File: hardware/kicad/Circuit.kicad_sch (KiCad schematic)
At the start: 10 parts, among them J1 TYPE-C-31-M-12, U1 ESP32-C6-WROOM-1-N8, U2 BME680, U3 BQ24075RGT

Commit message: hardware: power section & components
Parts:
- removed U2: BME680, BME680:PSON80P300X300X100-8N, symbol SnapEDA-Library:BME680
- added C10: 22uF, PCM_JLCPCB:C_0603, symbol Device:C
- added C2: 100nF, PCM_JLCPCB:C_0603, symbol Device:C
- added C3, C4, C8, C9: 10uF, PCM_JLCPCB:C_0603, symbol Device:C
- added C5, C7: 4.7uF, PCM_JLCPCB:C_0603, symbol Device:C
- added C6: 1uF, PCM_JLCPCB:C_0603, symbol Device:C
- added D3, D6, D7, D8: LESD5D5.0CT1G, LESD5D5.0CT1G:TVS_LESD5D5.0CT1G, symbol LESD5D5.0CT1G:LESD5D5.0CT1G
- added D4: 1N5819HW-7-F, 1N5819HW-7-F:SOD3715X145N, symbol 1N5819HW-7-F:1N5819HW-7-F
- added D5: Red, PCM_JLCPCB:D_0603, symbol PCM_JLCPCB-Diodes:LED,0603,Red
- added D9: Green, PCM_JLCPCB:D_0603, symbol PCM_JLCPCB-Diodes:LED,0603,Red
- added J2: B2B-XH-A__LF__SN_, B2B-XH-A__LF__SN_:JST_B2B-XH-A__LF__SN_, symbol B2B-XH-A__LF__SN_:B2B-XH-A__LF__SN_
- added L1: 1.5uH, Inductor_SMD:L_0603_1608Metric, symbol Device:L
- added R10: 470K, PCM_JLCPCB:R_0603, symbol Device:R
- added R11: 150K, PCM_JLCPCB:R_0603, symbol Device:R
- added R12: R, PCM_JLCPCB:R_0603, symbol Device:R
- added R4: 887, PCM_JLCPCB:R_0603, symbol Device:R
- added R5: 1.1K, PCM_JLCPCB:R_0603, symbol Device:R
- added R6, R9: 5k1, PCM_JLCPCB:R_0603, symbol Device:R
- added R7, R8: 1.5K, PCM_JLCPCB:R_0603, symbol Device:R
- added TH1: 10K, Resistor_SMD:R_0603_1608Metric, symbol Device:Thermistor_NTC
- added U4: TPS63070RNMR, TPS63070RNMR:VREG_TPS63070RNMR, symbol TPS63070RNMR:TPS63070RNMR
- added U5: BME680, BME680:PSON80P300X300X100-8N, symbol BME680:BME680
- R2: value 5k1 -> R
- R3: value 5k1 -> 10K
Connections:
- net VBUS is gone; now on net +5V: J1.A4_B9 (VBUS), J1.B4_A9 (VBUS)
- net GND: now also U3.14 (TMR), U3.15 (SYSOFF), U3.17 (VSS), U3.4 (~{CE}), U3.6 (EN1), U3.8 (VSS), C10.2, C2.2, C3.1, C4.2, C5.2, C6.2, C7.1, C8.2, C9.2, D6.1, D7.1, D8.1, J2.2, R11.2, R4.1, R5.1, R6.2, R9.2, TH1.2, U4.10 (PGND), U4.15 (VSEL), U4.4 (GND), U4.6 (FB2), U5.1 (GND), U5.7 (GND); no longer R2.2, R3.2
- net TS: now reaches U3.1 (TS)
- net TS: now also TH1.1
- net OUT: now reaches U3.10 (OUT), U3.11 (OUT)
- net OUT: now also R3.1, C4.1, C5.1, C8.1, D5.2, D9.2, U4.12_13 (VIN)
- net at U3.12 (ILIM): now also R5.2
- net +5V: now reaches U3.13 (IN)
- net +5V: now also U3.5 (EN2), C3.2, C6.1, C7.2, D6.2
- net at U3.16 (ISET): now also R4.2
- net BAT: now reaches U3.2 (BAT), U3.3 (BAT)
- net BAT: now also J2.1
- net ~{PGOOD}: now reaches U3.7 (~{PGOOD})
- net ~{PGOOD}: now also R8.2
- net ~{CHG}: now reaches U3.9 (~{CHG})
- net ~{CHG}: now also R7.2
- net at R2.1: no longer J1.A5 (CC1)
- net D+: now reaches J1.A6 (DP1), J1.B6 (DP2)
- net D+: now also D8.2
- net D-: now reaches J1.A7 (DN1), J1.B7 (DN2)
- net D-: now also D7.2
- net CC2: now reaches J1.B5 (CC2)
- net CC2: now also R6.1; no longer R3.1
- new net: D5.1, R7.1
- new net: L1.2, U4.11 (L1)
- new net: C2.1, U4.3 (VAUX)
- new net: L1.1, U4.9 (L2)
- new net: D9.1, R8.1
- new net +3.3V: C10.1, C9.1, R10.1, R12.1, U4.7_8 (VOUT)
- new net CC1: J1.A5 (CC1), R9.1
- new net EN: R3.2, U4.1 (PS/SYNC), U4.14 (EN)
- new net FB: R10.2, R11.1, U4.5 (FB)
- new net PG: R12.2, U4.2 (PG)
- no-connect marks 0 -> 2
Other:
- note added: "1N5819HW-7-F not needed, BQ24075RGT is equiped with reverse current protecion on IN pin"
- note added: "Battery connector"
- note added: "Battery current limited to 500 mA"
- note added: "Buck boost converter"
- note added: "Check pins of battery, change polarization if needed"
- note added: "Dynamic Power Path Management"
- note added: "Enviroment sensor"
- note added: "Input current limited to 1500 mA"
- note added: "MCU"
- note added: "Max operating current 3A"
- note added: "On battery connector: JST SYP-02T-1"
- note added: "Output = 3.3V"
- note added: "R4 Tollerance must be 1%"
- note added: "TH1 must be close to J2"
- note added: "Test point"
- note added: "USB-C"
- company: (none) -> Glitch Projects
- title: (none) -> Weather station
- moved on the sheet: C1, D1, D2, J1, R1, U1, U3

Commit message: hardware: MCU components
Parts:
- removed C1: C, PCM_JLCPCB:C_0603, symbol Device:C
- removed D1: 1N5819, Diode_THT:D_DO-41_SOD81_P10.16mm_Horizontal, symbol Diode:1N5819
- removed D2: Red, PCM_JLCPCB:D_0603, symbol PCM_JLCPCB-Diodes:LED,0603,Red
- removed D3: LESD5D5.0CT1G, LESD5D5.0CT1G:TVS_LESD5D5.0CT1G, symbol LESD5D5.0CT1G:LESD5D5.0CT1G
- removed D4: 1N5819HW-7-F, 1N5819HW-7-F:SOD3715X145N, symbol 1N5819HW-7-F:1N5819HW-7-F
- removed R1, R2: R, PCM_JLCPCB:R_0603, symbol Device:R
- removed U1: ESP32-C6-WROOM-1-N8, ESP32-C6-WROOM-1-N8:XCVR_ESP32-C6-WROOM-1-N8, symbol SnapEDA-Library:ESP32-C6-WROOM-1-N8
- removed U5: BME680, BME680:PSON80P300X300X100-8N, symbol BME680:BME680
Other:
- note removed: "Enviroment sensor"
- note removed: "MCU"

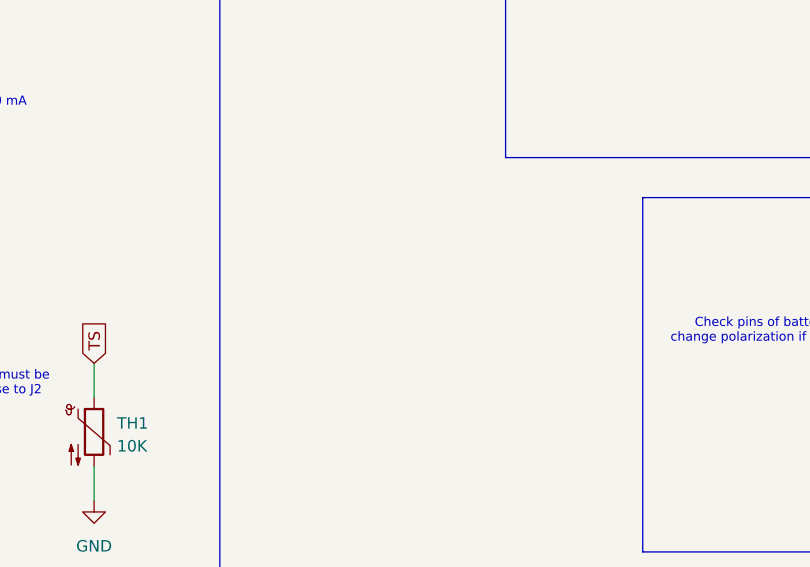
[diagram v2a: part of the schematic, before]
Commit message: hardware: movement sensor
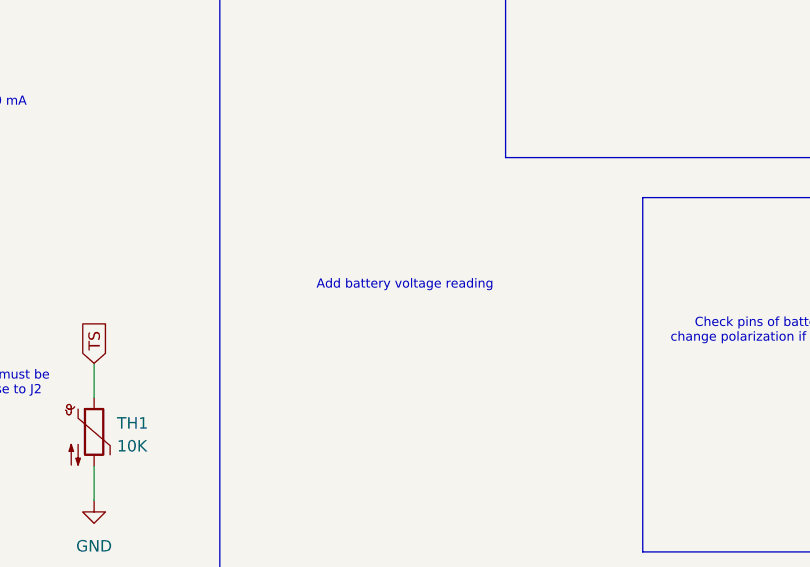
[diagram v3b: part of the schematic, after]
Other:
- note added: "Add battery voltage reading"
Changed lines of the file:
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@@
+		)
+	)
+	(text "Add battery voltage reading"
+		(exclude_from_sim yes)
+		(at 151.384 128.524 0)
+		(effects
+			(font
+				(size 1.016 1.016)
+			)
 		)
 	)

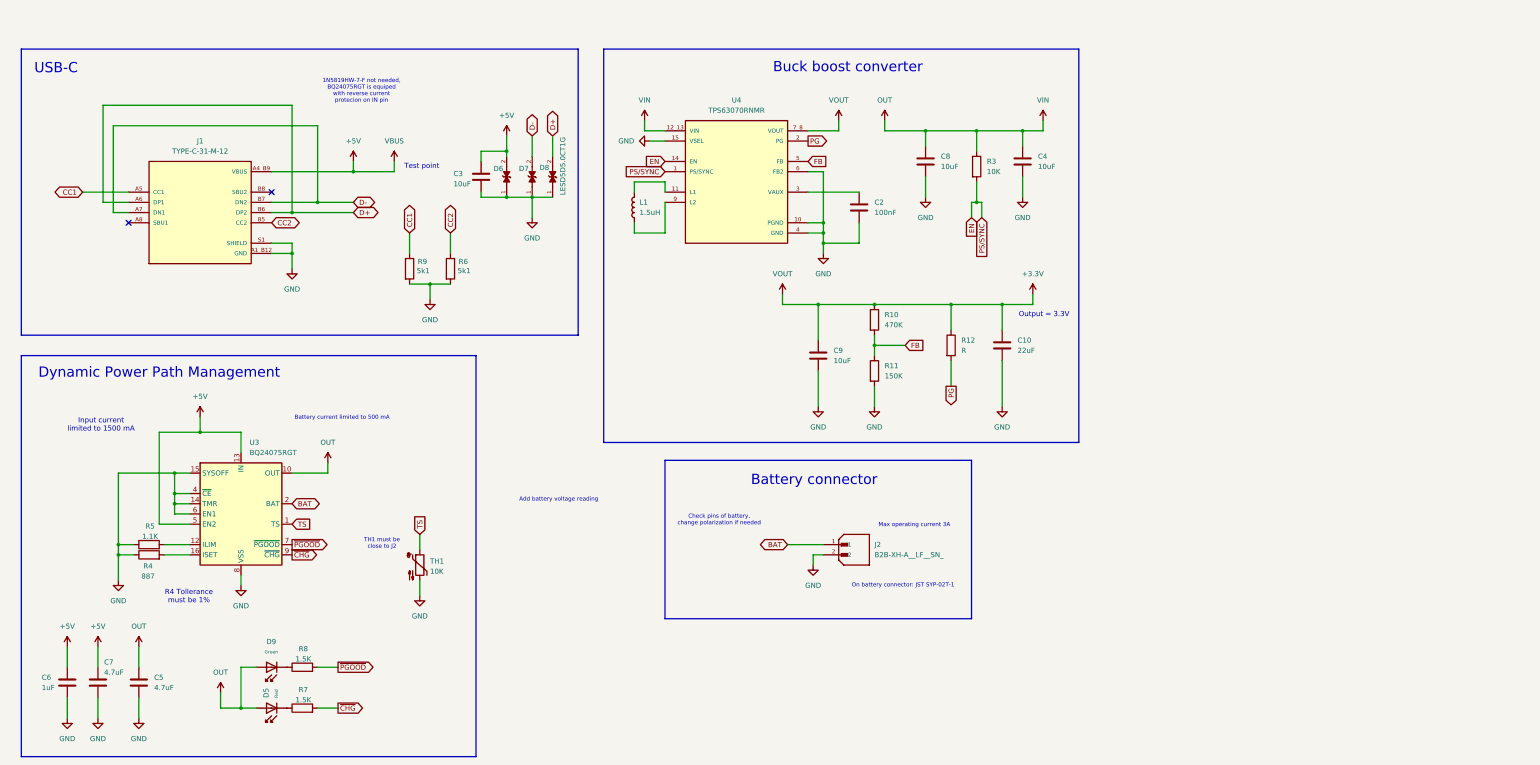
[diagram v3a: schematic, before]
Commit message: hardware: battery voltage reading and caps
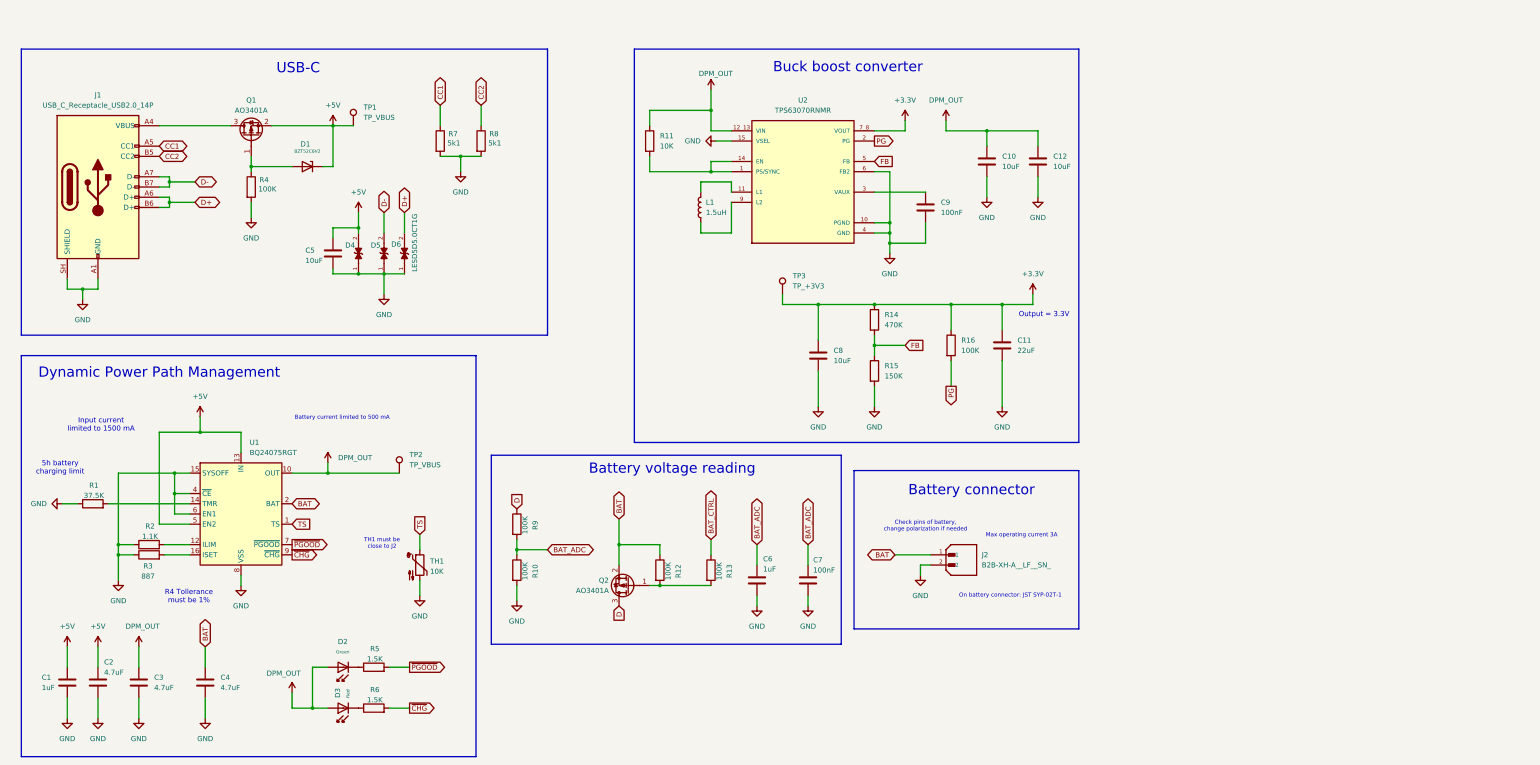
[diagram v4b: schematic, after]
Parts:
- removed J1: TYPE-C-31-M-12, TYPE-C-31-M-12:HRO_TYPE-C-31-M-12, symbol TYPE-C-31-M-12:TYPE-C-31-M-12
- added C4: 4.7uF, PCM_JLCPCB:C_0603, symbol Device:C
- added C6: 1uF, PCM_JLCPCB:C_0603, symbol Device:C
- added C7: 100nF, PCM_JLCPCB:C_0603, symbol Device:C
- added D1: BZT52C6V2, PCM_JLCPCB:D_SOD-123, symbol PCM_JLCPCB-Diodes:Zener,BZT52C6V2
- added J1: USB_C_Receptacle_USB2.0_14P, Connector_USB:USB_C_Receptacle_HRO_TYPE-C-31-M-12, symbol Connector:USB_C_Receptacle_USB2.0_14P
- added Q1, Q2: AO3401A, Package_TO_SOT_SMD:SOT-23, symbol Transistor_FET:AO3401A
- added R1: 37.5K, PCM_JLCPCB:R_0603, symbol Device:R
- added R10, R12, R13, R4, R9: 100K, PCM_JLCPCB:R_0603, symbol Device:R
- added TP1, TP2: TP_VBUS, TestPoint:TestPoint_Pad_D1.5mm, symbol Connector:TestPoint
- added TP3: TP_+3V3, TestPoint:TestPoint_Pad_D1.5mm, symbol Connector:TestPoint
- D4: renamed from D6; footprint LESD5D5.0CT1G:TVS_LESD5D5.0CT1G -> Diode_SMD:TVS_LESD5D5.0CT1G
- D5: renamed from D7; footprint LESD5D5.0CT1G:TVS_LESD5D5.0CT1G -> Diode_SMD:TVS_LESD5D5.0CT1G
- D6: renamed from D8; footprint LESD5D5.0CT1G:TVS_LESD5D5.0CT1G -> Diode_SMD:TVS_LESD5D5.0CT1G
- J2: footprint B2B-XH-A__LF__SN_:JST_B2B-XH-A__LF__SN_ -> Connector_JST:JST_B2B-XH-A__LF__SN_
- R16: renamed from R12; value R -> 100K
- U2: renamed from U4; footprint TPS63070RNMR:VREG_TPS63070RNMR -> Converter_DCDC:VREG_TPS63070RNMR
- renumbered C6 to C1, C8 to C10, C10 to C11, C4 to C12, C7 to C2, C5 to C3, C3 to C5, C9 to C8, C2 to C9, D9 to D2, D5 to D3, R3 to R11, R10 to R14, R11 to R15, R5 to R2, R4 to R3, R8 to R5, R7 to R6, R9 to R7, R6 to R8, U3 to U1
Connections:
- net +3.3V: now also TP3.1
- net +5V: now also D1.1, Q1.2 (S), TP1.1
- net BAT: now also C4.1, Q2.2 (S), R12.1
- net CC1: now also J1.A5 (CC1)
- net CC2: now also J1.B5 (CC2)
- net D+: now also J1.A6 (D+), J1.B6 (D+)
- net D-: now also J1.A7 (D-), J1.B7 (D-)
- net GND: now also C4.2, C6.1, C7.1, J1.A1 (GND), J1.A12 (GND), J1.B1 (GND), J1.B12 (GND), J1.SH (SHIELD), R1.1, R10.2, R4.2; no longer U1.14 (TMR)
- net EN: no longer names the net of R11.2, U2.1 (PS/SYNC), U2.14 (EN)
- net OUT renamed DPM_OUT
- net DPM_OUT: now also TP2.1
- new net: R1.2, U1.14 (TMR)
- new net: Q2.1 (G), R12.2, R13.2
- new net: D1.2, Q1.1 (G), R4.1
- new net: J1.A4 (VBUS), J1.A9 (VBUS), J1.B4 (VBUS), J1.B9 (VBUS), Q1.3 (D)
- new net BAT_ADC: C6.2, C7.2, R10.1, R9.2
- new net BAT_CTRL: R13.1
- new net D: Q2.3 (D), R9.1
- no-connect marks 2 -> 0
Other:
- note added: "5h battery charging limit"
- note added: "Battery voltage reading"
- note removed: "1N5819HW-7-F not needed, BQ24075RGT is equiped with reverse current protecion on IN pin"
- note removed: "Add battery voltage reading"
- note removed: "Test point"
- company: Glitch Projects -> Glitch
- title: Weather station -> Weather station - Power section
- moved on the sheet: C10, C12, C5, C9, D2, D3, D4, D5, D6, J2, L1, R11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

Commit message: hardware: modfied wiring
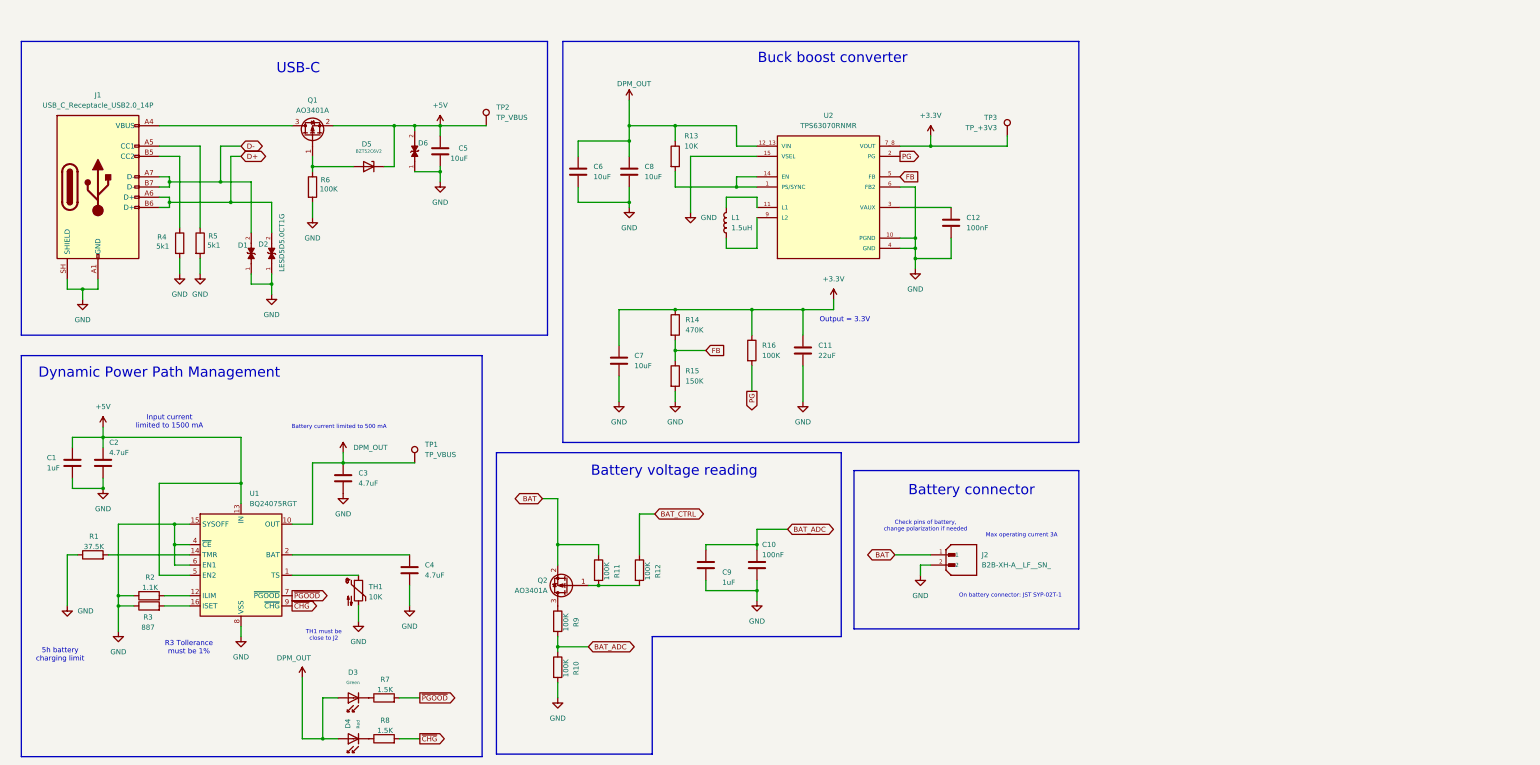
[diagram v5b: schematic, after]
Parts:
- renumbered C7 to C10, C9 to C12, C10 to C6, C8 to C7, C12 to C8, C6 to C9, D5 to D1, D6 to D2, D2 to D3, D3 to D4, D1 to D5, D4 to D6, R12 to R11, R13 to R12, R11 to R13, R7 to R4, R8 to R5, R4 to R6, R5 to R7, R6 to R8, TP2 to TP1, TP1 to TP2
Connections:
- net BAT: no longer C4.1, U1.2 (BAT), U1.3 (BAT)
- net CC1: no longer names the net of J1.A5 (CC1)
- net CC1: now also R5.1; no longer R4.1
- net CC2: no longer names the net of J1.B5 (CC2)
- net CC2: now also R4.1; no longer R5.1
- net D: no longer names the net of Q2.3 (D), R9.1
- net TS: no longer names the net of TH1.1, U1.1 (TS)
- new net: C4.1, U1.2 (BAT), U1.3 (BAT)
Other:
- note added: "R3 Tollerance must be 1%"
- note removed: "R4 Tollerance must be 1%"
- moved on the sheet: C1, C10, C11, C12, C2, C3, C4, C5, C6, C7, C8, C9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

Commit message: fix: incorrect values and missing wirings
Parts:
- added C4: 2.2uF, PCM_JLCPCB:C_0603, symbol Device:C
- C6: renamed from C5; value 10uF -> 2.2uF
- D1, D2: value LESD5D5.0CT1G -> PESD5V0X1UL
- D6: value LESD5D5.0CT1G -> ESD5Z6.8T1G
- L1: value 1.5uH -> 1.5uH 4A
- R1: value 37.5K -> 71.5K
- R2: value 1.1K -> 1.6K
- R3: value 887 -> 1.78K
- R6: value 100K -> 470K
- TP1: value TP_VBUS -> TP_SYS
- renumbered C9 to C10, C10 to C11, C11 to C12, C12 to C13, C4 to C5, C6 to C7, C7 to C8, C8 to C9
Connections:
- net +5V: no longer U1.5 (EN2)
- net BAT: now also C5.1, U1.2 (BAT), U1.3 (BAT)
- net GND: now also C4.1; no longer R2.1, R3.1, U1.15 (SYSOFF), U1.4 (~{CE}), U1.6 (EN1)
- net at D5.2, Q1.1 (G), R6.1: now also C4.2
- new net: R2.1, R3.1, U1.15 (SYSOFF), U1.4 (~{CE})
- new net CHG_EN1: U1.6 (EN1)
- new net CHG_EN2: U1.5 (EN2)
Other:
- moved on the sheet: D5, R1, R6
